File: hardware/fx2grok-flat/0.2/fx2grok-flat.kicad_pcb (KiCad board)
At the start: 4 copper layers, 40 x 20 mm, 38 parts, among them IC1 CY7C68013A-56, J1 Conn_02x05_Odd_Even, P1 pkl_USB_OTG, U1 3.3V, U2 USBLC6-2, U3 DSILC6-4, U4 DSILC6-4, U5 pkl_24LC00, X1 24MHz

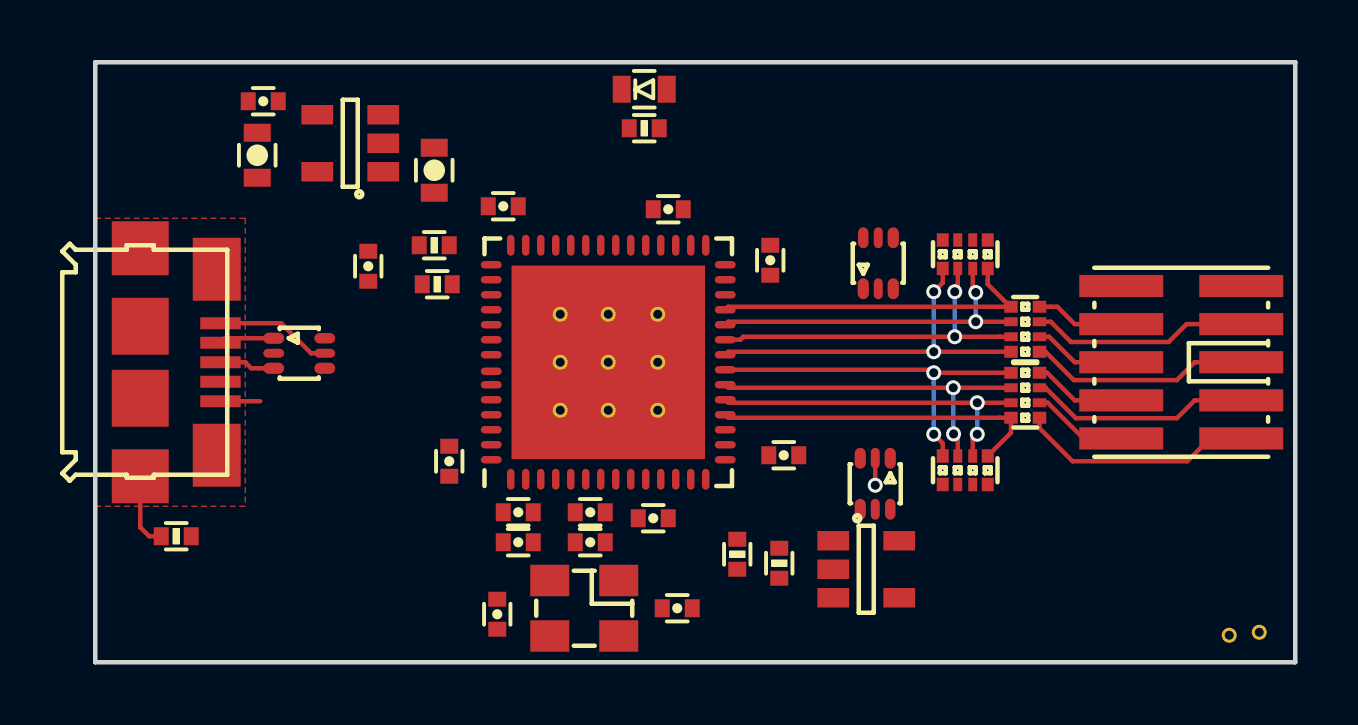
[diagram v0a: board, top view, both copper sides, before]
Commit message: FX2Grok-flat with new frontend first routing pass.
This is the status of the design as included on esden KiCad LP.
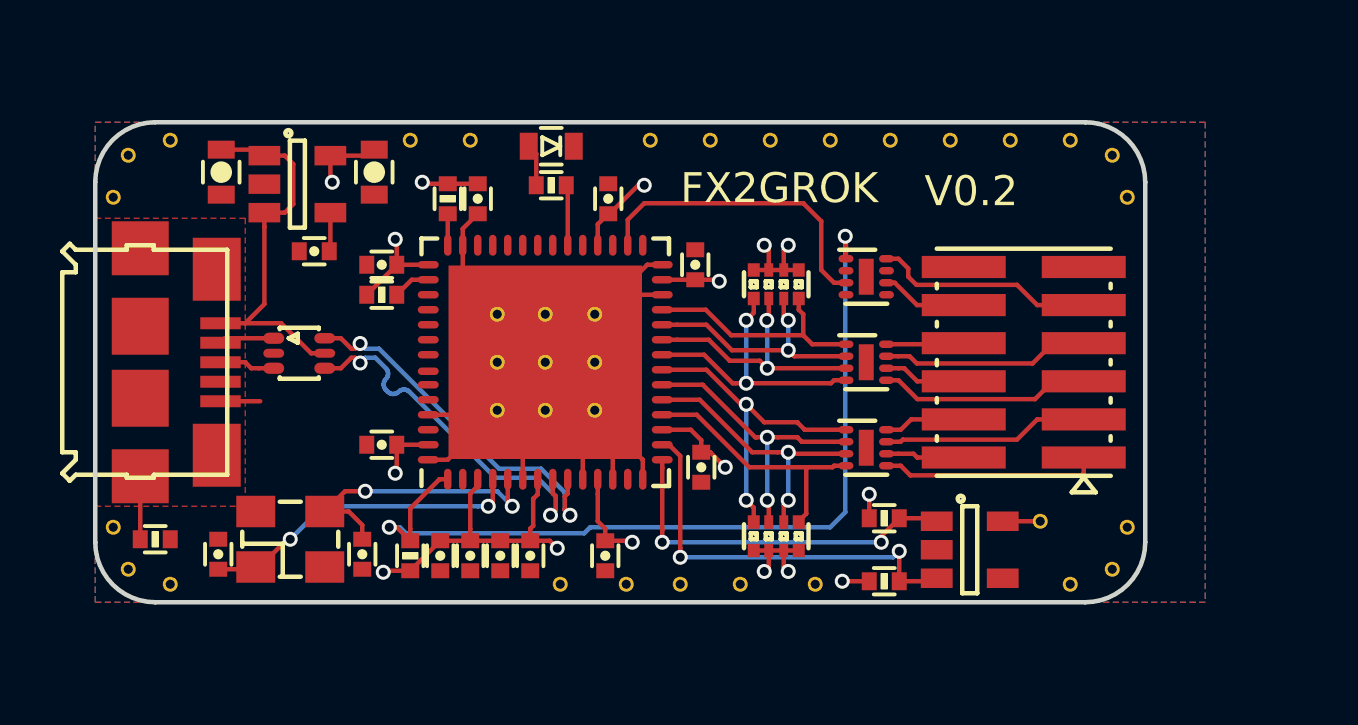
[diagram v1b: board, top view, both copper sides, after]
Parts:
- removed R7: 100E, pkl_dipol:R_Array_Convex_4x0402
- added REF**: via0305, pkl_misc:via0305, F.Cu at (32.5, 22.6)
- added REF**: via0305, pkl_misc:via0305, F.Cu at (52.5, 22.6)
- added REF**: via0305, pkl_misc:via0305, F.Cu at (53.9, 23.1)
- added REF**: via0305, pkl_misc:via0305, F.Cu at (54.4, 24.5)
- added REF**: via0305, pkl_misc:via0305, F.Cu at (53.9, 36.9)
- added REF**: via0305, pkl_misc:via0305, F.Cu at (22.5, 22.6)
- added REF**: via0305, pkl_misc:via0305, F.Cu at (21.1, 23.1)
- added REF**: via0305, pkl_misc:via0305, F.Cu at (20.6, 24.5)
- added REF**: via0305, pkl_misc:via0305, F.Cu at (20.6, 35.5)
- added REF**: via0305, pkl_misc:via0305, F.Cu at (21.1, 36.9)
- added REF**: via0305, pkl_misc:via0305, F.Cu at (22.5, 37.4)
- added REF**: via0305, pkl_misc:via0305, F.Cu at (30.5, 22.6)
- added REF**: via0305, pkl_misc:via0305, F.Cu at (35.5, 37.4)
- added REF**: via0305, pkl_misc:via0305, F.Cu at (37.7, 37.4)
- added REF**: via0305, pkl_misc:via0305, F.Cu at (39.5, 37.4)
- added REF**: via0305, pkl_misc:via0305, F.Cu at (41.5, 37.4)
- added REF**: via0305, pkl_misc:via0305, F.Cu at (44.0, 37.4)
- added REF**: via0305, pkl_misc:via0305, F.Cu at (52.5, 37.4)
- added REF**: via0305, pkl_misc:via0305, F.Cu at (38.5, 22.6)
- added REF**: via0305, pkl_misc:via0305, F.Cu at (40.5, 22.6)
- added REF**: via0305, pkl_misc:via0305, F.Cu at (42.5, 22.6)
- added REF**: via0305, pkl_misc:via0305, F.Cu at (44.5, 22.6)
- added REF**: via0305, pkl_misc:via0305, F.Cu at (46.5, 22.6)
- added REF**: via0305, pkl_misc:via0305, F.Cu at (48.5, 22.6)
- added REF**: via0305, pkl_misc:via0305, F.Cu at (50.5, 22.6)
- added U6: IP425x-4-TTL, pkl_housings_dfn_qfn:DFN-8-1EP_1.35x1.7mm_Pitch0.4mm, F.Cu at (45.7, 27.1)
- J1: footprint pkl_samtec:FTSH-105-XX-X-DV -> pkl_samtec:TFC-106-02-X-D
- R6: value 100E -> 100k; footprint pkl_dipol:R_Array_Convex_4x0402 -> pkl_dipol:R_0402
- U3, U4: value DSILC6-4 -> IP425x-4-TTL; footprint pkl_housings_sot:SOT-666 -> pkl_housings_dfn_qfn:DFN-8-1EP_1.35x1.7mm_Pitch0.4mm
- moved R6 21.2 mm to (30.5, 36.5)
- moved C16 10.7 mm to (28.9, 36.4), turned to 270 degrees
- moved X1 10.1 mm to (26.5, 35.9), turned to 0 degrees
- moved C15 9.51 mm to (24.1, 36.4)
- moved REF** 8.18 mm to (51.5, 35.3)
- moved C11 7.10 mm to (24.2, 23.7), turned to 270 degrees
- moved R8 6.67 mm to (42.7, 35.8)
- moved R9 6.38 mm to (42.7, 27.4)
- moved C12 5.28 mm to (27.3, 26.3)
- moved J1 5.25 mm to (51.0, 30.0)
- moved R3 4.98 mm to (46.3, 37.3), turned to 180 degrees
- moved REF** 4.95 mm to (54.4, 35.5)
- moved C5 4.49 mm to (29.6, 26.8), turned to 180 degrees
- moved C14 4.29 mm to (32.8, 24.6), turned to 270 degrees
- moved C13 3.94 mm to (29.3, 23.7), turned to 270 degrees
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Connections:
- IC1 pad 1: (no net) -> /TRIG
- IC1 pad 30: (no net) -> /CLK
- IC1 pad 33: /PA0 -> (no net)
- IC1 pad 34: (no net) -> /PA1
- IC1 pad 57: (no net) -> GND
- J1 pad 10: GND -> /xCLK
- J1 pad 9: GND -> /xTRIG
- R1 pad 2: /PA0 -> /PA1
- R6 pad 1: /xPB0 -> +3V3
- R6 pad 2: /PB0 -> /TRIG
- U3 pad 1: /PB0 -> /PB3
- U3 pad 2: GND -> /PB2
- U3 pad 3: /PB3 -> /PB1
- U3 pad 4: /PB2 -> /PB0
- U3 pad 5: +5V -> /xPB0
- U3 pad 6: /PB1 -> /xPB1
- U4 pad 1: /PB4 -> /PB7
- U4 pad 2: GND -> /PB6
- U4 pad 4: /PB7 -> /PB4
- U4 pad 5: +5V -> /xPB4
- U4 pad 6: /PB6 -> /xPB5
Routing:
- net +3V3: track 0.00 -> 40.2 mm, vias 0 -> 16
- net /TRIG: track 0.00 -> 29.1 mm, vias 0 -> 2
- net GND: track 2.22 -> 17.7 mm, vias 1 -> 0
- net /SDA: track 0.00 -> 13.8 mm, vias 0 -> 2
- net /USBD_P: track 0.00 -> 12.5 mm, vias 0 -> 2
- net /USBD_N: track 0.00 -> 12.4 mm, vias 0 -> 2
- net /SCL: track 0.00 -> 12.4 mm, vias 0 -> 2
- net /XTALOUT: track 0.00 -> 10.8 mm, vias 0 -> 2
- net /CLK: track 0.00 -> 10.4 mm
- net /XTALIN: track 0.00 -> 9.61 mm, vias 0 -> 2
- net +5V: track 3.89 -> 12.9 mm
- net /xTRIG: track 0.00 -> 7.37 mm
- net /PB7: track 11.2 -> 7.89 mm
- net /PB6: track 11.4 -> 8.35 mm
- net /PB5: track 11.9 -> 8.88 mm
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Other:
- board size 40 x 20 mm -> 35 x 16 mm
- net class Default: clearance 0.15 -> 0.149
- rule trace_clearance: 0.15 -> 0.149
- board text added: "FX2GROK"
- board text added: "V0.2"

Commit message: More cleanup of the board routing.
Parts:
- removed the REF** at (44.0, 37.4)
- removed the REF** at (51.5, 35.3)
- added REF**: via0305, pkl_misc:via0305, F.Cu at (50.5, 37.4)
- added REF**: via0305, pkl_misc:via0305, F.Cu at (26.5, 22.6)
- added REF**: via0305, pkl_misc:via0305, F.Cu at (28.5, 22.6)
- added REF**: via0305, pkl_misc:via0305, F.Cu at (36.5, 22.6)
- added REF**: via0305, pkl_misc:via0305, F.Cu at (34.5, 22.6)
- added REF**: via0305, pkl_misc:via0305, F.Cu at (26.5, 37.4)
- added REF**: via0305, pkl_misc:via0305, F.Cu at (28.5, 37.4)
- added REF**: via0305, pkl_misc:via0305, F.Cu at (30.5, 37.4)
- added REF**: via0305, pkl_misc:via0305, F.Cu at (32.5, 37.4)
- added REF**: via0305, pkl_misc:via0305, F.Cu at (48.5, 37.4)
- added REF**: via0305, pkl_misc:via0305, F.Cu at (34.5, 37.4)
- added REF**: via0305, pkl_misc:via0305, F.Cu at (46.5, 37.4)
- added REF**: via0305, pkl_misc:via0305, F.Cu at (44.5, 37.4)
- added REF**: via0305, pkl_misc:via0305, F.Cu at (52.9, 25.7)
- added REF**: via0305, pkl_misc:via0305, F.Cu at (49.0, 25.7)
- added REF**: via0305, pkl_misc:via0305, F.Cu at (45.7, 25.7)
- added REF**: via0305, pkl_misc:via0305, F.Cu at (45.7, 28.6)
- added REF**: via0305, pkl_misc:via0305, F.Cu at (45.7, 31.4)
- U3, U4, U6: footprint pkl_housings_dfn_qfn:DFN-8-1EP_1.35x1.7mm_Pitch0.4mm -> pkl_housings_dfn_qfn:DFN-8-1EP_1.35x1.7mm_Pitch0.45mm
- moved R2 8.34 mm to (38.0, 36.0), turned to 270 degrees
- moved R3 7.41 mm to (39.0, 36.0), turned to 270 degrees
- moved C15 5.69 mm to (28.0, 32.2)
- moved U5 3.12 mm to (46.1, 35.6)
- moved X1 2.53 mm to (28.9, 35.1), turned to 270 degrees
- moved U1 2.13 mm to (28.8, 24.6)
- moved C16 2.13 mm to (31.0, 36.0)
- moved C13 2.09 mm to (31.3, 24.3)
- moved P1 2.00 mm to (23.5, 30.0)
- moved R10 2.00 mm to (24.0, 35.9)
- moved REF** 2.00 mm to (24.5, 22.6)
- moved REF** 2.00 mm to (23.1, 23.1)
- moved REF** 2.00 mm to (22.6, 24.5)
- moved REF** 2.00 mm to (22.6, 35.5)
- moved REF** 2.00 mm to (23.1, 36.9)
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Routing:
- net /TRIG: track 29.1 -> 24.9 mm
- net /XTALOUT: track 10.8 -> 8.35 mm
- net /XTALIN: track 9.61 -> 7.40 mm
- net /CLK: track 10.4 -> 8.81 mm
- net /SDA: track 13.8 -> 12.3 mm
- net /USBD_P: track 12.5 -> 11.2 mm
- net /USBD_N: track 12.4 -> 11.2 mm
- net GND: track 17.7 -> 16.5 mm
- net Net-(C12-Pad1): track 1.30 -> 2.42 mm
- net +3V3: track 40.2 -> 39.2 mm, vias 16 -> 13
- net /PA1: track 2.02 -> 1.19 mm
- net /PB3: track 11.0 -> 10.4 mm
- net +5V: track 12.9 -> 12.3 mm
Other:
- board size 35 x 16 mm -> 33 x 16 mm
- board text added: "0"
- board text added: "2"
- board text added: "3"
- board text added: "4"
- board text added: "5"
- board text added: "6"
- board text added: "7"
- board text added: "C"
- board text added: "G"
- board text added: "T"

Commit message: Final cleanup before placing prototype order.
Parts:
- added REF**: via0305, pkl_misc:via0305, F.Cu at (28.9, 33.9)
- added REF**: via0305, pkl_misc:via0305, F.Cu at (30.0, 31.0)
- U3, U4, U6: footprint pkl_housings_dfn_qfn:DFN-8-1EP_1.35x1.7mm_Pitch0.45mm -> pkl_housings_dfn_qfn:DFN-8-1EP_1.35x1.7mm_Pitch0.4mm
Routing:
- net +3V3: track 39.2 -> 40.6 mm
- net GND: track 16.5 -> 17.5 mm, vias 0 -> 1
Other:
- board text added: "1"
- board text added: "FX2Grok Flat"
- board text added: "Flat"
- board text added: "V2.0 CC-BY-SA 4.0"

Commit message: Placement plan layout.
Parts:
- D1: value pkl_LED -> GRN
- U5: value pkl_24LC00 -> 24LC00

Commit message: Minor value adjustment.
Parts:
- added REF**: 1b2_Logo_SilkS_10mm, pkl_logos:1b2_Logo_SilkS_10mm, B.Cu at (39.5, 30.0)
- C15, C16: value 12p -> 10p
- R10: value 2k7 -> 1m
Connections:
- C14 pad 1: +3V3 -> /~RESET
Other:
- board text added: "1BitSquared"
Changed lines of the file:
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@@
   (general
     (links 200)
-    (no_connects 0)
+    (no_connects 1)
     (area 20.326 17.3 64.85 40.593405)
     (thickness 1.6)
-    (drawings 54)
+    (drawings 55)
     (tracks 409)
     (zones 0)
-    (modules 81)
+    (modules 82)
     (nets 38)
   )
@@
     (add_net "Net-(D1-PadA)")
   )
+  (module pkl_logos:1b2_Logo_SilkS_10mm (layer B.Cu)
+    (at 39.5 30 90)
+    (fp_text reference REF** (at 0 -6 90) (layer B.Fab) hide
+      (effects (font (size 1 1) (thickness 0.15)) (justify mirror))
+    )
+    (fp_text value 1b2_Logo_SilkS_10mm (at 0 6.35 90) (layer B.Fab) hide
+      (effects (font (size 1 1) (thickness 0.15)) (justify mirror))
+    )
+    (fp_line (start -3 -5) (end 5 -5) (layer B.SilkS) (width 0.4))
+    (fp_line (start -4 -4) (end -3 -5) (layer B.SilkS) (width 0.4))
+    (fp_line (start 5 -5) (end 4 -4) (layer B.SilkS) (width 0.4))
+    (fp_line (start 5 3) (end 5 -5) (layer B.SilkS) (width 0.4))
+    (fp_line (start 4 4) (end 5 3) (layer B.SilkS) (width 0.4))
+    (fp_line (start 4 -4) (end 4 4) (layer B.SilkS) (width 0.4))
+    (fp_line (start -4 -4) (end 4 -4) (layer B.SilkS) (width 0.4))
+    (fp_line (start -4 -1) (end -4 -4) (layer B.SilkS) (width 0.4))
+    (fp_line (start 1 -1) (end -4 -1) (layer B.SilkS) (width 0.4))
+    (fp_line (start 1 4) (end 1 -1) (layer B.SilkS) (width 0.4))
+    (fp_line (start 4 4) (end 1 4) (layer B.SilkS) (width 0.4))
+    (fp_line (start -4 0) (end 0 0) (layer B.SilkS) (width 0.4))
+    (fp_line (start -5 1) (end -4 0) (layer B.SilkS) (width 0.4))
+    (fp_line (start 0 0) (end -1 1) (layer B.SilkS) (width 0.4))
+    (fp_line (start 0 4) (end 0 0) (layer B.SilkS) (width 0.4))
+    (fp_line (start -1 5) (end 0 4) (layer B.SilkS) (width 0.4))
+    (fp_line (start -5 1) (end -1 1) (layer B.SilkS) (width 0.4))
+    (fp_line (start -5 5) (end -5 1) (layer B.SilkS) (width 0.4))
+    (fp_line (start -1 5) (end -5 5) (layer B.SilkS) (width 0.4))
+    (fp_line (start -1 1) (end -1 5) (layer B.SilkS) (width 0.4))
+  )
   (module pkl_misc:via0305 (layer F.Cu)
     (at 28.9 33.9)
@@
     (fp_line (start 0.35 0.44) (end -0.35 0.44) (layer F.SilkS) (width 0.13))
     (pad 1 smd rect (at -0.5 0 270) (size 0.5 0.6) (layers F.Cu F.Paste F.Mask)
-      (net 1 +3V3))
+      (net 15 /~RESET))
     (pad 2 smd rect (at 0.5 0 270) (size 0.5 0.6) (layers F.Cu F.Paste F.Mask)
       (net 2 GND))
@@
       (effects (font (size 0.635 0.635) (thickness 0.1)))
     )
-    (fp_text value 12p (at 0 1 90) (layer F.Fab)
+    (fp_text value 10p (at 0 1 90) (layer F.Fab)
       (effects (font (size 0.635 0.635) (thickness 0.1)))
     )
@@
       (effects (font (size 0.635 0.635) (thickness 0.1)))
     )
-    (fp_text value 12p (at 2.95 0 270) (layer F.Fab)
+    (fp_text value 10p (at 2.95 0 270) (layer F.Fab)
       (effects (font (size 0.635 0.635) (thickness 0.1)))
     )
@@
       (effects (font (size 0.635 0.635) (thickness 0.1)))
     )
-    (fp_text value 2k7 (at 1.85 0) (layer F.Fab)
+    (fp_text value 1m (at 1.85 0) (layer F.Fab)
       (effects (font (size 0.635 0.635) (thickness 0.1)))
     )
@@
     )
   )
+  (gr_text 1BitSquared (at 32.2 30 270) (layer B.SilkS)
+    (effects (font (size 1.5 1.5) (thickness 0.3)) (justify mirror))
+  )
   (gr_text Flat (at 42.2 25.4) (layer F.SilkS)
